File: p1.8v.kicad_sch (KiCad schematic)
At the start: 11 parts, among them U12 LT3045xDD

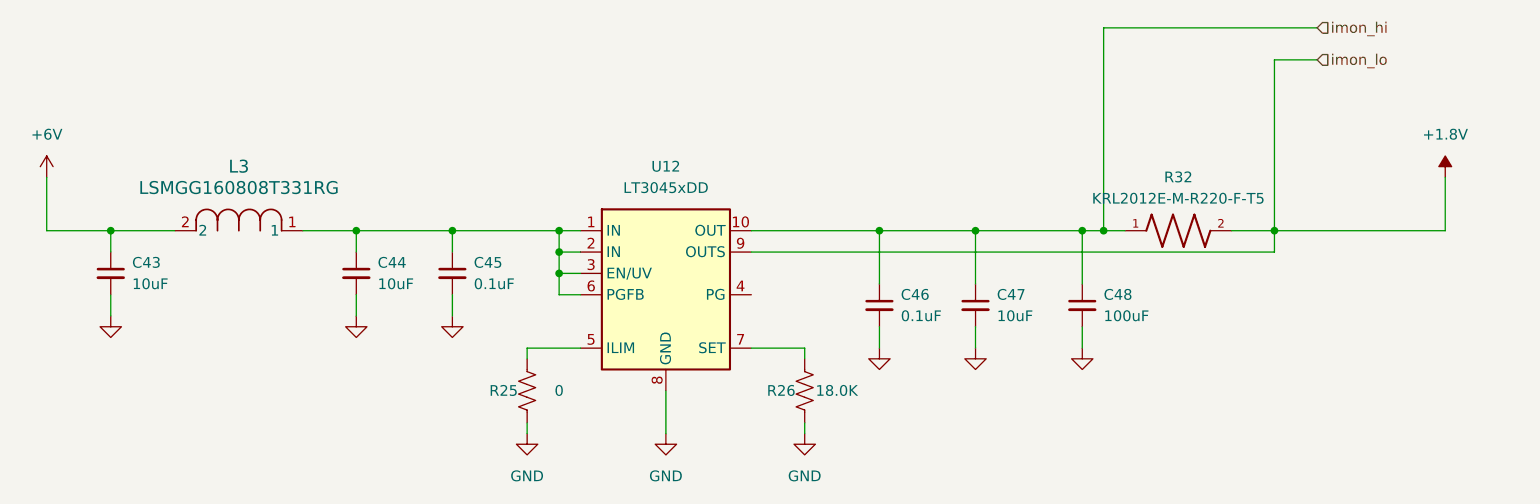
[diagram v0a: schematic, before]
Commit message: Add all 4 channels
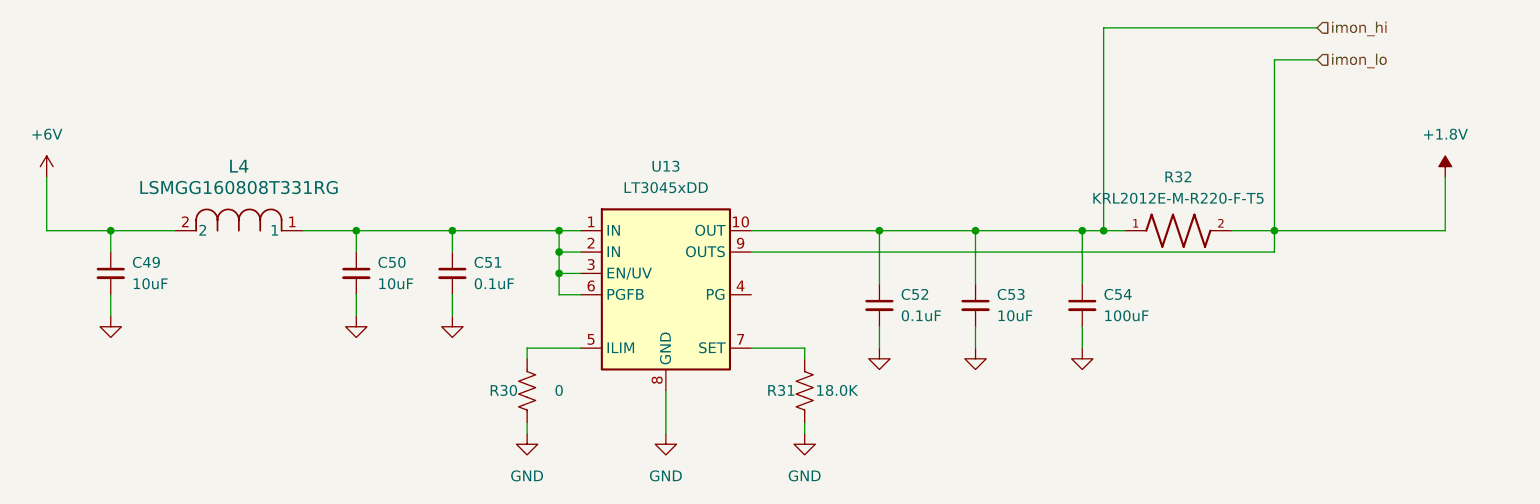
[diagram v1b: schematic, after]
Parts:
- renumbered C43 to C49, C44 to C50, C45 to C51, C46 to C52, C47 to C53, C48 to C54, L3 to L4, R25 to R30, R26 to R31, U12 to U13
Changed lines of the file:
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@@
 		(on_board yes)
 		(dnp no)
-		(property "Reference" "C45"
+		(property "Reference" "C51"
 			(at 121.92 74.9362 0)
 			(effects
@@
 			(project "psc_carrier_brd"
 				(path "/40891cc8-bf64-41f4-8f69-a607d7b280eb/d1842e08-6ad7-4891-bdb3-3a3a498e2a30/1b238acc-ea4e-4f24-9d93-142263e92f3e"
-					(reference "C45")
+					(reference "C51")
 					(unit 1)
 				)
@@
 		(on_board yes)
 		(dnp no)
-		(property "Reference" "C47"
+		(property "Reference" "C53"
 			(at 184.15 78.7462 0)
 			(effects
@@
 			(project "psc_carrier_brd"
 				(path "/40891cc8-bf64-41f4-8f69-a607d7b280eb/d1842e08-6ad7-4891-bdb3-3a3a498e2a30/1b238acc-ea4e-4f24-9d93-142263e92f3e"
-					(reference "C47")
+					(reference "C53")
 					(unit 1)
 				)
@@
 		(dnp no)
 		(fields_autoplaced yes)
-		(property "Reference" "U12"
+		(property "Reference" "U13"
 			(at 144.78 63.5 0)
 			(effects
@@
 			(project ""
 				(path "/40891cc8-bf64-41f4-8f69-a607d7b280eb/d1842e08-6ad7-4891-bdb3-3a3a498e2a30/1b238acc-ea4e-4f24-9d93-142263e92f3e"
-					(reference "U12")
+					(reference "U13")
 					(unit 1)
 				)
@@
 		(dnp no)
 		(fields_autoplaced yes)
-		(property "Reference" "#PWR0104"
+		(property "Reference" "#PWR0120"
 			(at 128.27 101.6 0)
 			(effects
@@
 			(project "psc_carrier_brd"
 				(path "/40891cc8-bf64-41f4-8f69-a607d7b280eb/d1842e08-6ad7-4891-bdb3-3a3a498e2a30/1b238acc-ea4e-4f24-9d93-142263e92f3e"
-					(reference "#PWR0104")
+					(reference "#PWR0120")
 					(unit 1)
 				)
@@
 		(on_board yes)
 		(dnp no)
-		(property "Reference" "C43"
+		(property "Reference" "C49"
 			(at 81.28 74.9362 0)
 			(effects
@@
 			(project "psc_carrier_brd"
 				(path "/40891cc8-bf64-41f4-8f69-a607d7b280eb/d1842e08-6ad7-4891-bdb3-3a3a498e2a30/1b238acc-ea4e-4f24-9d93-142263e92f3e"
-					(reference "C43")
+					(reference "C49")
 					(unit 1)
 				)
@@
 		(on_board yes)
 		(dnp no)
-		(property "Reference" "C48"
+		(property "Reference" "C54"
 			(at 196.85 78.7462 0)
 			(effects
@@
 			(project "psc_carrier_brd"
 				(path "/40891cc8-bf64-41f4-8f69-a607d7b280eb/d1842e08-6ad7-4891-bdb3-3a3a498e2a30/1b238acc-ea4e-4f24-9d93-142263e92f3e"
-					(reference "C48")
+					(reference "C54")
 					(unit 1)
 				)
@@
 		(dnp no)
 		(fields_autoplaced yes)
-		(property "Reference" "#PWR0105"
+		(property "Reference" "#PWR0121"
 			(at 144.78 101.6 0)
 			(effects
@@
 			(project ""
 				(path "/40891cc8-bf64-41f4-8f69-a607d7b280eb/d1842e08-6ad7-4891-bdb3-3a3a498e2a30/1b238acc-ea4e-4f24-9d93-142263e92f3e"
-					(reference "#PWR0105")
+					(reference "#PWR0121")
 					(unit 1)
 				)
@@
 		(dnp no)
 		(fields_autoplaced yes)
-		(property "Reference" "#PWR0107"
+		(property "Reference" "#PWR0123"
 			(at 170.18 91.44 0)
 			(effects
@@
 			(project "psc_carrier_brd"
 				(path "/40891cc8-bf64-41f4-8f69-a607d7b280eb/d1842e08-6ad7-4891-bdb3-3a3a498e2a30/1b238acc-ea4e-4f24-9d93-142263e92f3e"
-					(reference "#PWR0107")
+					(reference "#PWR0123")
 					(unit 1)
 				)
@@
 		(on_board yes)
 		(dnp no)
-		(property "Reference" "R25"
+		(property "Reference" "R30"
 			(at 125.476 90.17 0)
 			(effects
@@
 			(project "psc_carrier_brd"
 				(path "/40891cc8-bf64-41f4-8f69-a607d7b280eb/d1842e08-6ad7-4891-bdb3-3a3a498e2a30/1b238acc-ea4e-4f24-9d93-142263e92f3e"
-					(reference "R25")
+					(reference "R30")
 					(unit 1)
 				)
@@
 		(dnp no)
 		(fields_autoplaced yes)
-		(property "Reference" "#PWR0110"
+		(property "Reference" "#PWR0126"
 			(at 237.49 68.58 0)
 			(effects
@@
 			(project ""
 				(path "/40891cc8-bf64-41f4-8f69-a607d7b280eb/d1842e08-6ad7-4891-bdb3-3a3a498e2a30/1b238acc-ea4e-4f24-9d93-142263e92f3e"
-					(reference "#PWR0110")
+					(reference "#PWR0126")
 					(unit 1)
 				)
@@
 		(dnp no)
 		(fields_autoplaced yes)
-		(property "Reference" "#PWR0106"
+		(property "Reference" "#PWR0122"
 			(at 161.29 101.6 0)
 			(effects
@@
 			(project "psc_carrier_brd"
 				(path "/40891cc8-bf64-41f4-8f69-a607d7b280eb/d1842e08-6ad7-4891-bdb3-3a3a498e2a30/1b238acc-ea4e-4f24-9d93-142263e92f3e"
-					(reference "#PWR0106")
+					(reference "#PWR0122")
 					(unit 1)
 				)
@@
 		(on_board yes)
 		(dnp no)
-		(property "Reference" "C46"
+		(property "Reference" "C52"
 			(at 172.72 78.7462 0)
 			(effects
@@
 			(project "psc_carrier_brd"
 				(path "/40891cc8-bf64-41f4-8f69-a607d7b280eb/d1842e08-6ad7-4891-bdb3-3a3a498e2a30/1b238acc-ea4e-4f24-9d93-142263e92f3e"
-					(reference "C46")
+					(reference "C52")
 					(unit 1)
 				)
@@
 		(dnp no)
 		(fields_autoplaced yes)
-		(property "Reference" "#PWR0101"
+		(property "Reference" "#PWR0117"
 			(at 78.74 87.63 0)
 			(effects
@@
 			(project "psc_carrier_brd"
 				(path "/40891cc8-bf64-41f4-8f69-a607d7b280eb/d1842e08-6ad7-4891-bdb3-3a3a498e2a30/1b238acc-ea4e-4f24-9d93-142263e92f3e"
-					(reference "#PWR0101")
+					(reference "#PWR0117")
 					(unit 1)
 				)
@@
 		(dnp no)
 		(fields_autoplaced yes)
-		(property "Reference" "#PWR0109"
+		(property "Reference" "#PWR0125"
 			(at 194.31 91.44 0)
 			(effects
@@
 			(project "psc_carrier_brd"
 				(path "/40891cc8-bf64-41f4-8f69-a607d7b280eb/d1842e08-6ad7-4891-bdb3-3a3a498e2a30/1b238acc-ea4e-4f24-9d93-142263e92f3e"
-					(reference "#PWR0109")
+					(reference "#PWR0125")
 					(unit 1)
 				)
@@
 		(dnp no)
 		(fields_autoplaced yes)
-		(property "Reference" "#PWR0102"
+		(property "Reference" "#PWR0118"
 			(at 107.95 87.63 0)
 			(effects
@@
 			(project "psc_carrier_brd"
 				(path "/40891cc8-bf64-41f4-8f69-a607d7b280eb/d1842e08-6ad7-4891-bdb3-3a3a498e2a30/1b238acc-ea4e-4f24-9d93-142263e92f3e"
-					(reference "#PWR0102")
+					(reference "#PWR0118")
 					(unit 1)
 				)
@@
 		(on_board yes)
 		(dnp no)
-		(property "Reference" "R26"
+		(property "Reference" "R31"
 			(at 158.496 90.17 0)
 			(effects
@@
 			(project "psc_carrier_brd"
 				(path "/40891cc8-bf64-41f4-8f69-a607d7b280eb/d1842e08-6ad7-4891-bdb3-3a3a498e2a30/1b238acc-ea4e-4f24-9d93-142263e92f3e"
-					(reference "R26")
+					(reference "R31")
 					(unit 1)
 				)
@@
 		(dnp no)
 		(fields_autoplaced yes)
-		(property "Reference" "#PWR0103"
+		(property "Reference" "#PWR0119"
 			(at 119.38 87.63 0)
 			(effects
@@
 			(project "psc_carrier_brd"
 				(path "/40891cc8-bf64-41f4-8f69-a607d7b280eb/d1842e08-6ad7-4891-bdb3-3a3a498e2a30/1b238acc-ea4e-4f24-9d93-142263e92f3e"
-					(reference "#PWR0103")
+					(reference "#PWR0119")
 					(unit 1)
 				)
@@
 		(dnp no)
 		(fields_autoplaced yes)
-		(property "Reference" "L3"
+		(property "Reference" "L4"
 			(at 93.98 63.5 0)
 			(effects
@@
 			(project ""
 				(path "/40891cc8-bf64-41f4-8f69-a607d7b280eb/d1842e08-6ad7-4891-bdb3-3a3a498e2a30/1b238acc-ea4e-4f24-9d93-142263e92f3e"
-					(reference "L3")
+					(reference "L4")
 					(unit 1)
 				)
@@
 		(dnp no)
 		(fields_autoplaced yes)
-		(property "Reference" "#PWR0100"
+		(property "Reference" "#PWR0116"
 			(at 71.12 68.58 0)
 			(effects
@@
 			(project ""
 				(path "/40891cc8-bf64-41f4-8f69-a607d7b280eb/d1842e08-6ad7-4891-bdb3-3a3a498e2a30/1b238acc-ea4e-4f24-9d93-142263e92f3e"
-					(reference "#PWR0100")
+					(reference "#PWR0116")
 					(unit 1)
 				)
@@
 		(on_board yes)
 		(dnp no)
-		(property "Reference" "C44"
+		(property "Reference" "C50"
 			(at 110.49 74.9362 0)
 			(effects
@@
 			(project "psc_carrier_brd"
 				(path "/40891cc8-bf64-41f4-8f69-a607d7b280eb/d1842e08-6ad7-4891-bdb3-3a3a498e2a30/1b238acc-ea4e-4f24-9d93-142263e92f3e"
-					(reference "C44")
+					(reference "C50")
 					(unit 1)
 				)
@@
 		(dnp no)
 		(fields_autoplaced yes)
-		(property "Reference" "#PWR0108"
+		(property "Reference" "#PWR0124"
 			(at 181.61 91.44 0)
 			(effects
@@
 			(project "psc_carrier_brd"
 				(path "/40891cc8-bf64-41f4-8f69-a607d7b280eb/d1842e08-6ad7-4891-bdb3-3a3a498e2a30/1b238acc-ea4e-4f24-9d93-142263e92f3e"
-					(reference "#PWR0108")
-					(unit 1)
-				)
+					(reference "#PWR0124")
+					(unit 1)
+				)

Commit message: Start routing
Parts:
- renumbered C49 to C34, C50 to C35, C51 to C36, C52 to C37, C53 to C38, C54 to C39, R30 to R20, R31 to R21, R32 to R22, U13 to U9
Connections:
- net +6V renamed +5.0V
- no-connect marks 0 -> 1

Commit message: Finished layout
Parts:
- added TP6: ${SHORT_NET_NAME(1)}, TestPoint:TestPoint_THTPad_D2.0mm_Drill1.0mm, symbol Connector:TestPoint
- C34, C35, C38: Cost (none) -> .04; MFG (none) -> Samsung; MFG_PN (none) -> CL10A106MA8NRNC
- C36, C37: Cost (none) -> .01; MFG (none) -> Taiyo Yuden; MFG_PN (none) -> TMK105BJ104KV-F
- C39: Cost (none) -> 0.22; MFG (none) -> Murata; MFG_PN (none) -> GRM31CR61A107MEA8L
- L4: Cost (none) -> .01; MFG (none) -> Taiyo Yuden; MFG_PN (none) -> LSMGG160808T331RG
- R20: Cost (none) -> 0.01; MFG (none) -> Panasonic; MFG_PN (none) -> ERJ-2GE0R00X
- R21: Cost (none) -> 0.01; MFG (none) -> Panasonic; MFG_PN (none) -> ERJ-2RKF1802X
- R22: value KRL2012E-M-R220-F-T5 -> 0.22; Cost (none) -> 0.38; MFG (none) -> Susumu; MFG_PN (none) -> KRL2012E-M-R220-F-T5
- U9: Cost (none) -> 6.06; MFG (none) -> Analog Devices; MFG_PN (none) -> LT3045EDD#TRPBF
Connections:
- net +1.8V: now also TP6.1
- net Vin_1.8v: now reaches C35.1, C36.1, L4.1, U9.1 (IN), U9.2 (IN), U9.6 (PGFB)
- net Vin_1.8v: no longer U9.3 (EN/UV)
- new net enb: U9.3 (EN/UV)
